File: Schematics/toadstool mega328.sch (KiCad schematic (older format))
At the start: 25 parts, among them CON1 BARREL_JACK, IC1 ATMEGA328P-P, K1 CAP, K2 V-SELECT, K4 ICSP, K5 PIN 2-8, K6 PIN 21-28, K7 XTAL, K8 PIN 15-19, K9 PIN 11-14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

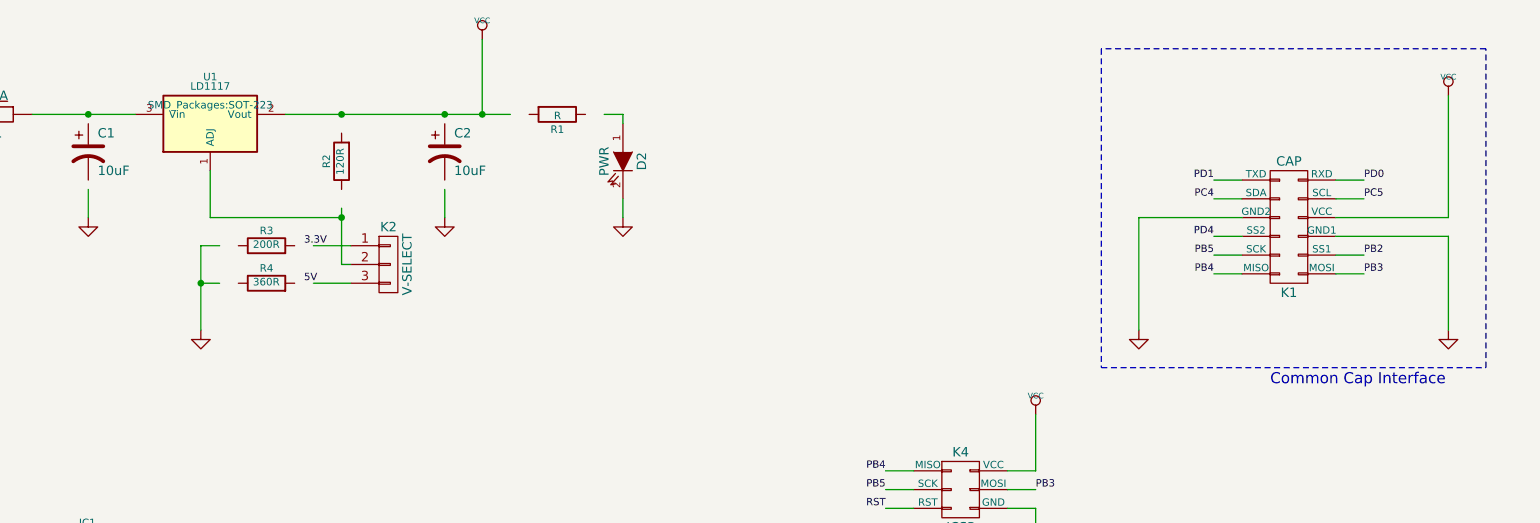
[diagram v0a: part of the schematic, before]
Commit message: Cap Header
Widening of Cap Header
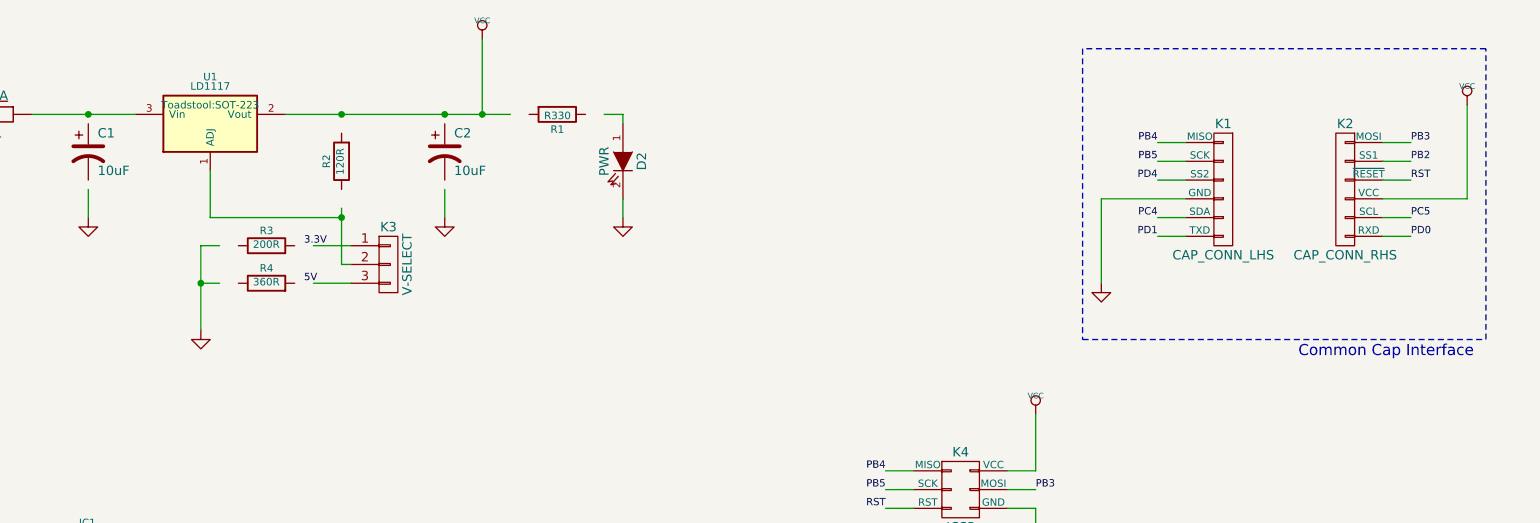
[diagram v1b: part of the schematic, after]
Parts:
- removed K1: CAP, Socket_Strips:Socket_Strip_Straight_2x06, symbol SHIELD_CONN
- added K1: CAP_CONN_LHS, Toadstool:Socket_Strip_Straight_1x06, symbol CAP_CONN_LHS
- added K2: CAP_CONN_RHS, Toadstool:Socket_Strip_Straight_1x06, symbol CAP_CONN_RHS
- D1: footprint Discret:D3 -> Toadstool:Diode_D3
- R1: value R -> R330
- U1: footprint SMD_Packages:SOT-223 -> Toadstool:SOT-223
- renumbered K2 to K3
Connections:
- wire segments 115 -> 114
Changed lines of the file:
@@
 Title "Toadstool Mega328"
 Date ""
-Rev "0.2"
+Rev "0.3"
 Comp "Crash-Bang Prototyping"
 Comment1 ""
@@
 Comment4 ""
 $EndDescr
-$Comp
-L SHIELD_CONN K1
-U 1 1 546E30CC
-P 9950 1750
-F 0 "K1" H 9950 2100 50  0000 C CNN
-F 1 "CAP" H 9950 1400 50  0000 C CNN
-F 2 "Socket_Strips:Socket_Strip_Straight_2x06" H 9950 550 60  0001 C CNN
-F 3 "" H 9950 550 60  0000 C CNN
-	1    9950 1750
-	-1   0    0    1
-$EndComp
 $Comp
 L ATMEGA328P-P IC1
@@
 F 0 "D1" H 2350 1250 40  0000 C CNN
 F 1 "DIODE" H 2350 1050 40  0000 C CNN
-F 2 "Discret:D3" H 2350 1150 60  0001 C CNN
+F 2 "Toadstool:Diode_D3" H 2350 1150 60  0001 C CNN
 F 3 "" H 2350 1150 60  0000 C CNN
 	1    2350 1150
@@
 $EndComp
 $Comp
-L CONN_01X03 K2
+L CONN_01X03 K3
 U 1 1 546E3889
 P 5150 1950
-F 0 "K2" H 5150 2150 50  0000 C CNN
+F 0 "K3" H 5150 2150 50  0000 C CNN
 F 1 "V-SELECT" V 5250 1950 50  0000 C CNN
 F 2 "Pin_Headers:Pin_Header_Straight_1x03" H 5150 1950 60  0001 C CNN
@@
 F 0 "U1" H 4200 1450 40  0000 C CNN
 F 1 "LD1117" H 4200 1400 40  0000 C CNN
-F 2 "SMD_Packages:SOT-223" H 4200 1300 40  0000 C CNN
+F 2 "Toadstool:SOT-223" H 4200 1300 40  0000 C CNN
 F 3 "" H 4200 1200 60  0000 C CNN
 	1    4200 1200
@@
 P 6050 1150
 F 0 "R1" V 6130 1150 40  0000 C CNN
-F 1 "R" V 6057 1151 40  0000 C CNN
+F 1 "R330" V 6057 1151 40  0000 C CNN
 F 2 "Resistors_SMD:R_0805" V 5980 1150 30  0001 C CNN
 F 3 "" H 6050 1150 30  0000 C CNN
@@
 $EndComp
 $Comp
-L VCC #PWR010
-U 1 1 5470E117
-P 10800 1050
-F 0 "#PWR010" H 10800 1150 30  0001 C CNN
-F 1 "VCC" H 10800 1150 30  0000 C CNN
-F 2 "" H 10800 1050 60  0000 C CNN
-F 3 "" H 10800 1050 60  0000 C CNN
-	1    10800 1050
-	1    0    0    -1
-$EndComp
-$Comp
-L GND #PWR011
-U 1 1 5470E229
-P 10800 2300
-F 0 "#PWR011" H 10800 2300 30  0001 C CNN
-F 1 "GND" H 10800 2230 30  0001 C CNN
-F 2 "" H 10800 2300 60  0000 C CNN
-F 3 "" H 10800 2300 60  0000 C CNN
-	1    10800 2300
-	1    0    0    -1
-$EndComp
-$Comp
-L GND #PWR012
-U 1 1 5470E283
-P 9150 2300
-F 0 "#PWR012" H 9150 2300 30  0001 C CNN
-F 1 "GND" H 9150 2230 30  0001 C CNN
-F 2 "" H 9150 2300 60  0000 C CNN
-F 3 "" H 9150 2300 60  0000 C CNN
-	1    9150 2300
-	1    0    0    -1
-$EndComp
-$Comp
 L R R5
 U 1 1 5470E6D6
@@
 $EndComp
 $Comp
-L VCC #PWR013
+L VCC #PWR010
 U 1 1 5470E832
 P 6300 4850
-F 0 "#PWR013" H 6300 4950 30  0001 C CNN
+F 0 "#PWR010" H 6300 4950 30  0001 C CNN
 F 1 "VCC" H 6300 4950 30  0000 C CNN
 F 2 "" H 6300 4850 60  0000 C CNN
@@
 $EndComp
 $Comp
-L GND #PWR014
+L GND #PWR011
 U 1 1 54720A7D
 P 3000 6450
-F 0 "#PWR014" H 3000 6450 30  0001 C CNN
+F 0 "#PWR011" H 3000 6450 30  0001 C CNN
 F 1 "GND" H 3000 6380 30  0001 C CNN
 F 2 "" H 3000 6450 60  0000 C CNN
@@
 Text Label 8600 3150 0    39   ~ 0
 PB3
-Text Label 10350 2000 0    39   ~ 0
-PB3
-Text Label 9550 2000 2    39   ~ 0
-PB4
-Text Label 9550 1900 2    39   ~ 0
-PB5
-Text Label 9550 1600 2    39   ~ 0
-PC4
-Text Label 9550 1500 2    39   ~ 0
-PD1
-Text Label 10350 1500 0    39   ~ 0
-PD0
-Text Label 10350 1600 0    39   ~ 0
-PC5
 Text Label 8050 4300 2    39   ~ 0
 PD0
@@
 PD4
 $Comp
-L VCC #PWR015
+L VCC #PWR012
 U 1 1 5473EC95
 P 7700 4600
-F 0 "#PWR015" H 7700 4700 30  0001 C CNN
+F 0 "#PWR012" H 7700 4700 30  0001 C CNN
 F 1 "VCC" H 7700 4700 30  0000 C CNN
 F 2 "" H 7700 4600 60  0000 C CNN
@@
 $EndComp
 $Comp
-L GND #PWR016
+L GND #PWR013
 U 1 1 5473F4A2
 P 7700 5050
-F 0 "#PWR016" H 7700 5050 30  0001 C CNN
+F 0 "#PWR013" H 7700 5050 30  0001 C CNN
 F 1 "GND" H 7700 4980 30  0001 C CNN
 F 2 "" H 7700 5050 60  0000 C CNN
@@
 PC5
 $Comp
-L GND #PWR017
+L GND #PWR014
 U 1 1 5474069E
 P 10700 5050
-F 0 "#PWR017" H 10700 5050 30  0001 C CNN
+F 0 "#PWR014" H 10700 5050 30  0001 C CNN
 F 1 "GND" H 10700 4980 30  0001 C CNN
 F 2 "" H 10700 5050 60  0000 C CNN
@@
 	8600 3250 8600 3600
 Wire Wire Line
-	10800 1050 10800 1700
-Wire Wire Line
-	10800 1700 10200 1700
-Wire Wire Line
-	10200 1800 10800 1800
-Wire Wire Line
-	10800 1800 10800 2300
-Wire Wire Line
-	9700 1700 9150 1700
-Wire Wire Line
-	9150 1700 9150 2300
-Wire Wire Line
 	6300 5100 6300 4850
 Wire Wire Line
@@
 Wire Wire Line
 	8450 3150 8600 3150
-Wire Wire Line
-	10200 1500 10350 1500
-Wire Wire Line
-	10200 1600 10350 1600
-Wire Wire Line
-	10200 1900 10350 1900
-Wire Wire Line
-	10200 2000 10350 2000
-Wire Wire Line
-	9700 2000 9550 2000
-Wire Wire Line
-	9700 1900 9550 1900
-Wire Wire Line
-	9700 1800 9550 1800
-Wire Wire Line
-	9700 1600 9550 1600
-Wire Wire Line
-	9700 1500 9550 1500
 Wire Wire Line
 	8150 4300 8050 4300
@@
 XTAL2
 $Comp
-L GND #PWR018
+L GND #PWR015
 U 1 1 54741461
 P 6550 4550
-F 0 "#PWR018" H 6550 4550 30  0001 C CNN
+F 0 "#PWR015" H 6550 4550 30  0001 C CNN
 F 1 "GND" H 6550 4480 30  0001 C CNN
 F 2 "" H 6550 4550 60  0000 C CNN
@@
 	6350 4350 6550 4350
 Connection ~ 6550 4350
-Text Label 9550 1800 2    39   ~ 0
-PD4
-Text Label 10350 1900 0    39   ~ 0
-PB2
 Wire Notes Line
-	11000 2500 11000 800
+	11000 2350 11000 800
 Wire Notes Line
-	11000 800  8950 800
+	11000 800  8850 800
 Wire Notes Line
-	8950 800  8950 2500
+	8850 800  8850 2350
 Wire Notes Line
-	8950 2500 11000 2500
-Text Notes 9850 2600 0    59   ~ 0
+	8850 2350 11000 2350
+Text Notes 10000 2450 0    59   ~ 0
 Common Cap Interface
 Text Label 3250 4100 2    39   ~ 0
@@
 Connection ~ 5700 5100
 $Comp
-L GND #PWR019
+L GND #PWR016
 U 1 1 54749718
 P 6300 5750
-F 0 "#PWR019" H 6300 5750 30  0001 C CNN
+F 0 "#PWR016" H 6300 5750 30  0001 C CNN
 F 1 "GND" H 6300 5680 30  0001 C CNN
 F 2 "" H 6300 5750 60  0000 C CNN
@@
 Connection ~ 3000 5700
 Connection ~ 3000 5800
+$Comp
+L CAP_CONN_RHS K2
+U 1 1 5511B5B6
+P 10250 1550
+F 0 "K2" H 10250 1900 50  0000 C CNN
+F 1 "CAP_CONN_RHS" H 10250 1200 50  0000 C CNN
+F 2 "Toadstool:Socket_Strip_Straight_1x06" H 10250 350 60  0001 C CNN
+F 3 "" H 10250 350 60  0000 C CNN
+	1    10250 1550
+	1    0    0    -1
+$EndComp
+$Comp
+L CAP_CONN_LHS K1
+U 1 1 5511B90D
+P 9600 1550
+F 0 "K1" H 9600 1900 50  0000 C CNN
+F 1 "CAP_CONN_LHS" H 9600 1200 50  0000 C CNN
+F 2 "Toadstool:Socket_Strip_Straight_1x06" H 9600 350 60  0001 C CNN
+F 3 "" H 9600 350 60  0000 C CNN
+	1    9600 1550
+	1    0    0    -1
+$EndComp
+Wire Wire Line
+	9400 1300 9250 1300
+Wire Wire Line
+	9400 1400 9250 1400
+Wire Wire Line
+	9400 1500 9250 1500
+$Comp
+L GND #PWR017
+U 1 1 5511BB8D
+P 8950 2050
+F 0 "#PWR017" H 8950 2050 30  0001 C CNN
+F 1 "GND" H 8950 1980 30  0001 C CNN
+F 2 "" H 8950 2050 60  0000 C CNN
+F 3 "" H 8950 2050 60  0000 C CNN
+	1    8950 2050
+	1    0    0    -1
+$EndComp
+Wire Wire Line
+	9400 1600 8950 1600
+Wire Wire Line
+	8950 1600 8950 2050
+Wire Wire Line
+	9400 1700 9250 1700
+Wire Wire Line
+	9400 1800 9250 1800
+Wire Wire Line
+	10450 1300 10600 1300
+Wire Wire Line
+	10450 1400 10600 1400
+Wire Wire Line
+	10450 1500 10600 1500
+$Comp
+L VCC #PWR018
+U 1 1 5511C022
+P 10900 1100
+F 0 "#PWR018" H 10900 1200 30  0001 C CNN
+F 1 "VCC" H 10900 1200 30  0000 C CNN
+F 2 "" H 10900 1100 60  0000 C CNN
+F 3 "" H 10900 1100 60  0000 C CNN
+	1    10900 1100
+	1    0    0    -1
+$EndComp
+Wire Wire Line
+	10450 1600 10900 1600
+Wire Wire Line
+	10900 1600 10900 1100
+Wire Wire Line
+	10450 1700 10600 1700
+Wire Wire Line
+	10450 1800 10600 1800
+Text Label 10600 1300 0    39   ~ 0
+PB3
+Text Label 10600 1400 0    39   ~ 0
+PB2
+Text Label 10600 1500 0    39   ~ 0
+RST
+Text Label 10600 1700 0    39   ~ 0
+PC5
+Text Label 10600 1800 0    39   ~ 0
+PD0
+Text Label 9250 1300 2    39   ~ 0
+PB4
+Text Label 9250 1400 2    39   ~ 0
+PB5
+Text Label 9250 1700 2    39   ~ 0
+PC4
+Text Label 9250 1800 2    39   ~ 0
+PD1
+Text Label 9250 1500 2    39   ~ 0
+PD4
 $EndSCHEMATC

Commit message: Final Prototype Commit
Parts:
- C2: footprint toadstool:c_elec_4x5.3 -> Toadstool:c_elec_4x5.3
- C3, C4, C5: footprint SMD_Packages:SMD-0805 -> Capacitors_SMD:C_0805_HandSoldering
- CON1: footprint toadstool:BARREL_JACK_No_Slot -> Toadstool:BARREL_JACK_No_Slot
- F1: footprint toadstool:MiniSMDPTC-4532 -> Toadstool:MiniSMDPTC-4532
- IC1: footprint Sockets_DIP:DIP-28__300_ELL -> Toadstool:DIP-28_IC
- K3: footprint Pin_Headers:Pin_Header_Straight_1x03 -> Toadstool:Pin_Header_Straight_1x03
- R1, R2, R3, R4, R5: footprint Resistors_SMD:R_0805 -> Resistors_SMD:R_0805_HandSoldering
- SW1: footprint toadstool:SW_PUSH -> Toadstool:Switch_SMT_Alps_SKQGAxE010
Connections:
- wire segments 114 -> 118
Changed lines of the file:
@@
 F 0 "IC1" H 3500 5850 40  0000 L BNN
 F 1 "ATMEGA328P-P" H 4650 3200 40  0000 L BNN
-F 2 "Sockets_DIP:DIP-28__300_ELL" H 4250 4600 30  0000 C CIN
+F 2 "Toadstool:DIP-28_IC" H 4250 4600 30  0000 C CIN
 F 3 "" H 4250 4600 60  0000 C CNN
 	1    4250 4600
@@
 F 0 "CON1" H 1550 1500 60  0000 C CNN
 F 1 "BARREL_JACK" H 1550 1050 60  0000 C CNN
-F 2 "toadstool:BARREL_JACK_No_Slot" H 1550 1250 60  0001 C CNN
+F 2 "Toadstool:BARREL_JACK_No_Slot" H 1550 1250 60  0001 C CNN
 F 3 "" H 1550 1250 60  0000 C CNN
 	1    1550 1250
@@
 F 0 "F1" V 3100 1200 50  0000 C CNN
 F 1 "750mA" V 2900 1150 50  0000 C CNN
-F 2 "toadstool:MiniSMDPTC-4532" H 3000 1150 60  0001 C CNN
+F 2 "Toadstool:MiniSMDPTC-4532" H 3000 1150 60  0001 C CNN
 F 3 "" H 3000 1150 60  0000 C CNN
 	1    3000 1150
@@
 F 0 "C2" H 5500 1450 50  0000 L CNN
 F 1 "10uF" H 5500 1250 50  0000 L CNN
-F 2 "toadstool:c_elec_4x5.3" H 5450 1350 60  0001 C CNN
+F 2 "Toadstool:c_elec_4x5.3" H 5450 1350 60  0001 C CNN
 F 3 "" H 5450 1350 60  0000 C CNN
 	1    5450 1350
@@
 F 0 "K3" H 5150 2150 50  0000 C CNN
 F 1 "V-SELECT" V 5250 1950 50  0000 C CNN
-F 2 "Pin_Headers:Pin_Header_Straight_1x03" H 5150 1950 60  0001 C CNN
+F 2 "Toadstool:Pin_Header_Straight_1x03" H 5150 1950 60  0001 C CNN
 F 3 "" H 5150 1950 60  0000 C CNN
 	1    5150 1950
@@
 F 0 "R1" V 6130 1150 40  0000 C CNN
 F 1 "R330" V 6057 1151 40  0000 C CNN
-F 2 "Resistors_SMD:R_0805" V 5980 1150 30  0001 C CNN
+F 2 "Resistors_SMD:R_0805_HandSoldering" V 5980 1150 30  0001 C CNN
 F 3 "" H 6050 1150 30  0000 C CNN
 	1    6050 1150
@@
 F 0 "R3" V 4580 1850 40  0000 C CNN
 F 1 "200R" V 4507 1851 40  0000 C CNN
-F 2 "Resistors_SMD:R_0805" V 4430 1850 30  0001 C CNN
+F 2 "Resistors_SMD:R_0805_HandSoldering" V 4430 1850 30  0001 C CNN
 F 3 "" H 4500 1850 30  0000 C CNN
 	1    4500 1850
@@
 F 0 "R2" V 4980 1400 40  0000 C CNN
 F 1 "120R" V 4907 1401 40  0000 C CNN
-F 2 "Resistors_SMD:R_0805" V 4830 1400 30  0001 C CNN
+F 2 "Resistors_SMD:R_0805_HandSoldering" V 4830 1400 30  0001 C CNN
 F 3 "" H 4900 1400 30  0000 C CNN
 	1    4900 1400
@@
 F 0 "R4" V 4580 2050 40  0000 C CNN
 F 1 "360R" V 4507 2051 40  0000 C CNN
-F 2 "Resistors_SMD:R_0805" V 4430 2050 30  0001 C CNN
+F 2 "Resistors_SMD:R_0805_HandSoldering" V 4430 2050 30  0001 C CNN
 F 3 "" H 4500 2050 30  0000 C CNN
 	1    4500 2050
@@
 F 0 "C5" H 3000 4700 40  0000 L CNN
 F 1 "100nF" H 3006 4515 40  0000 L CNN
-F 2 "SMD_Packages:SMD-0805" H 3038 4450 30  0001 C CNN
+F 2 "Capacitors_SMD:C_0805_HandSoldering" H 3038 4450 30  0001 C CNN
 F 3 "" H 3000 4600 60  0000 C CNN
 	1    3000 4600
@@
 F 0 "R5" V 6130 5100 40  0000 C CNN
 F 1 "10k" V 6057 5101 40  0000 C CNN
-F 2 "Resistors_SMD:R_0805" V 5980 5100 30  0001 C CNN
+F 2 "Resistors_SMD:R_0805_HandSoldering" V 5980 5100 30  0001 C CNN
 F 3 "" H 6050 5100 30  0000 C CNN
 	1    6050 5100
@@
 F 0 "C4" H 6150 4450 40  0000 L CNN
 F 1 "22pF" H 6156 4265 40  0000 L CNN
-F 2 "SMD_Packages:SMD-0805" H 6188 4200 30  0001 C CNN
+F 2 "Capacitors_SMD:C_0805_HandSoldering" H 6188 4200 30  0001 C CNN
 F 3 "" H 6150 4350 60  0000 C CNN
 	1    6150 4350
@@
 F 0 "C3" H 6150 4050 40  0000 L CNN
 F 1 "22pF" H 6156 3865 40  0000 L CNN
-F 2 "SMD_Packages:SMD-0805" H 6188 3800 30  0001 C CNN
+F 2 "Capacitors_SMD:C_0805_HandSoldering" H 6188 3800 30  0001 C CNN
 F 3 "" H 6150 3950 60  0000 C CNN
 	1    6150 3950
@@
 	3250 1150 3800 1150
 Wire Wire Line
-	3550 1550 3550 1700
-Wire Wire Line
-	4600 1150 5800 1150
-Wire Wire Line
-	4750 1850 4950 1850
-Wire Wire Line
-	4750 2050 4950 2050
-Wire Wire Line
-	4250 1850 4150 1850
+	3550 1500 3550 1700
+Wire Wire Line
+	4600 1150 5900 1150
+Wire Wire Line
+	4650 1850 4950 1850
+Wire Wire Line
+	4650 2050 4950 2050
+Wire Wire Line
+	4150 1850 4350 1850
 Wire Wire Line
 	4150 1850 4150 2300
 Wire Wire Line
-	4250 2050 4150 2050
+	4150 2050 4350 2050
 Connection ~ 4150 2050
 Wire Wire Line
 	4900 1950 4950 1950
 Wire Wire Line
-	4900 1650 4900 1950
+	4900 1550 4900 1950
 Wire Wire Line
 	4900 1700 4200 1700
@@
 Connection ~ 4900 1150
 Wire Wire Line
-	5450 1700 5450 1550
+	5450 1500 5450 1700
 Connection ~ 5450 1150
 Wire Wire Line
-	6300 1150 6400 1150
+	6200 1150 6400 1150
 Wire Wire Line
 	6400 1150 6400 1200
@@
 	5700 4950 5700 5400
 Wire Wire Line
-	5700 5100 5800 5100
+	5700 5100 5900 5100
 Connection ~ 5700 4950
 Wire Wire Line
@@
 	8150 5300 8050 5300
 Wire Wire Line
-	5950 3950 5650 3950
+	5650 3950 6000 3950
 Wire Wire Line
 	5650 3950 5650 4100
@@
 	5650 4200 5650 4350
 Wire Wire Line
-	5650 4350 5950 4350
+	5650 4350 6000 4350
 Connection ~ 5650 4100
 Connection ~ 5650 4200
@@
 $EndComp
 Wire Wire Line
-	6350 3950 6550 3950
+	6300 3950 6550 3950
 Wire Wire Line
 	6550 3950 6550 4550
 Wire Wire Line
-	6350 4350 6550 4350
+	6300 4350 6550 4350
 Connection ~ 6550 4350
 Wire Notes Line
@@
 F 0 "SW1" H 6150 5510 50  0000 C CNN
 F 1 "RESET" H 6000 5320 50  0000 C CNN
-F 2 "toadstool:SW_PUSH" H 6000 5400 60  0001 C CNN
+F 2 "Toadstool:Switch_SMT_Alps_SKQGAxE010" H 6000 5400 60  0001 C CNN
 F 3 "" H 6000 5400 60  0000 C CNN
 	1    6000 5400
@@
 	6300 5400 6300 5750
 Wire Wire Line
-	3000 2900 3000 4400
+	3000 2900 3000 4450
 Wire Wire Line
 	3350 3500 3000 3500
@@
 Connection ~ 3000 3800
 Wire Wire Line
-	3000 4800 3000 6450
+	3000 4750 3000 6450
 Wire Wire Line
 	3000 5800 3350 5800
@@
 PD1
 Text Label 9250 1500 2    39   ~ 0
-PD4
+PD3
+Wire Wire Line
+	3550 1150 3550 1200
+Wire Wire Line
+	4900 1150 4900 1250
+Wire Wire Line
+	5450 1150 5450 1200
+Wire Wire Line
+	6200 5100 6300 5100
 $EndSCHEMATC
